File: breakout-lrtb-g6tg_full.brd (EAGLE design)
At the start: 27.9 x 14 mm, 11 parts

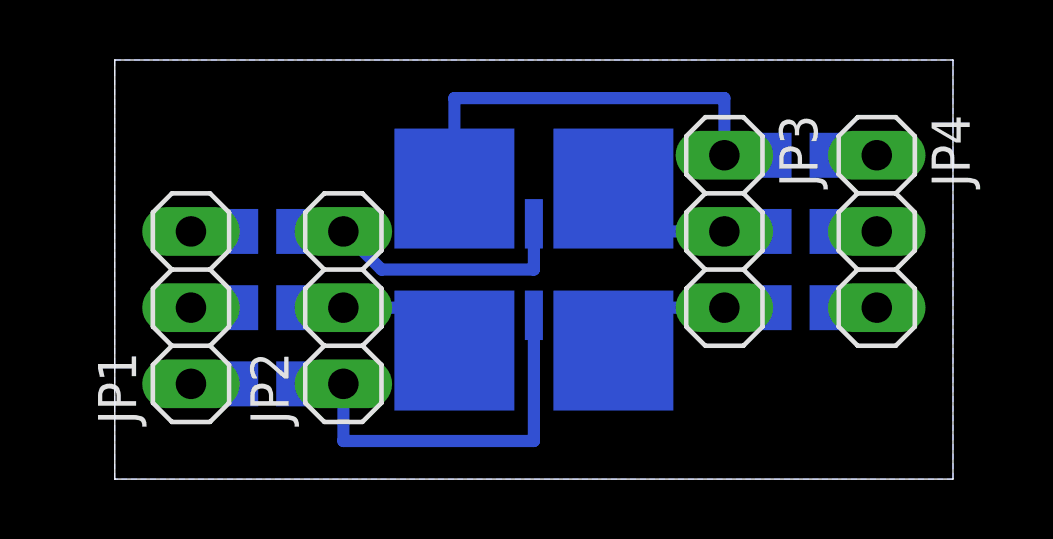
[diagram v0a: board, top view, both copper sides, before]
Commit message: another variant just with one pin for each pad
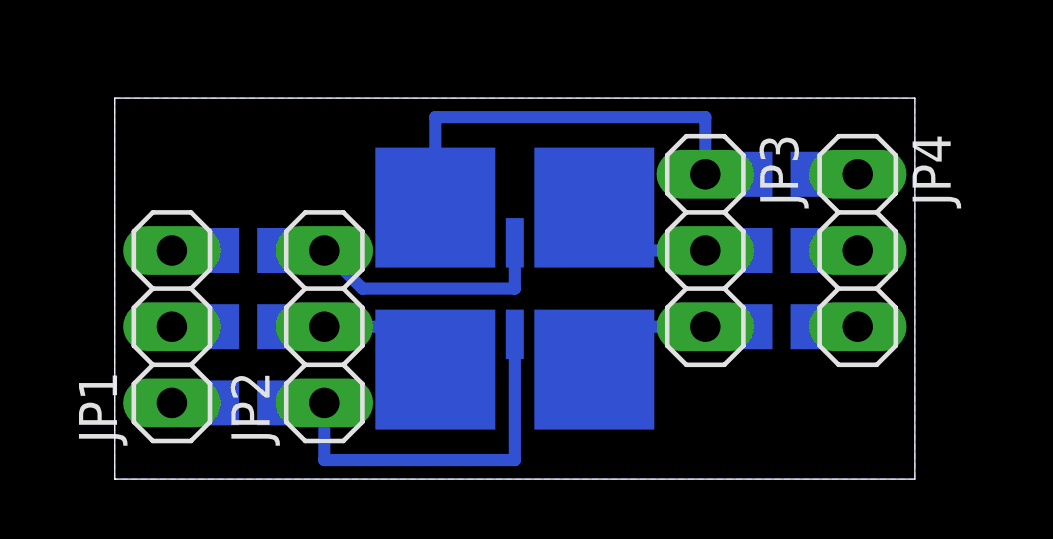
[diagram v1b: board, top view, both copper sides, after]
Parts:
- moved JP3 0.90 mm to (19.7, 7.62)
- moved LED1 0.90 mm to (13.3, 6.35)
- moved R1 0.90 mm to (4.45, 7.62)
- moved JP1 0.90 mm to (1.91, 5.08)
- moved JP2 0.90 mm to (6.99, 5.08)
- moved R2 0.90 mm to (4.45, 5.08)
- moved R3 0.90 mm to (4.45, 2.54)
- moved JP4 0.90 mm to (24.8, 7.62)
- moved R5 0.90 mm to (22.2, 7.62)
- moved R4 0.90 mm to (22.2, 5.08)
- moved R6 0.90 mm to (22.2, 10.2)
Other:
- board size 27.9 x 14 mm -> 26.7 x 12.7 mm
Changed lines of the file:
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@@
 <board>
 <plain>
-<wire x1="0" y1="0" x2="27.94" y2="0" width="0" layer="20"/>
-<wire x1="27.94" y1="0" x2="27.94" y2="13.97" width="0" layer="20"/>
-<wire x1="27.94" y1="13.97" x2="0" y2="13.97" width="0" layer="20"/>
-<wire x1="0" y1="13.97" x2="0" y2="0" width="0" layer="20"/>
-<rectangle x1="14.605" y1="6.35" x2="26.035" y2="7.62" layer="42"/>
-<rectangle x1="13.335" y1="9.525" x2="14.605" y2="12.065" layer="42"/>
-<rectangle x1="19.685" y1="8.89" x2="26.035" y2="10.16" layer="42"/>
-<rectangle x1="1.905" y1="6.35" x2="8.255" y2="7.62" layer="42"/>
-<rectangle x1="1.905" y1="3.81" x2="8.255" y2="5.08" layer="42"/>
+<wire x1="0" y1="0" x2="26.67" y2="0" width="0" layer="20"/>
+<wire x1="26.67" y1="0" x2="26.67" y2="12.7" width="0" layer="20"/>
+<wire x1="26.67" y1="12.7" x2="0" y2="12.7" width="0" layer="20"/>
+<wire x1="0" y1="12.7" x2="0" y2="0" width="0" layer="20"/>
+<rectangle x1="13.97" y1="5.715" x2="25.4" y2="6.985" layer="42"/>
+<rectangle x1="12.7" y1="8.89" x2="13.97" y2="11.43" layer="42"/>
+<rectangle x1="19.05" y1="8.255" x2="25.4" y2="9.525" layer="42"/>
+<rectangle x1="1.27" y1="5.715" x2="7.62" y2="6.985" layer="42"/>
+<rectangle x1="1.27" y1="3.175" x2="7.62" y2="4.445" layer="42"/>
+<rectangle x1="0.635" y1="1.27" x2="6.35" y2="1.905" layer="42"/>
+<rectangle x1="20.32" y1="11.43" x2="26.035" y2="12.065" layer="42"/>
 </plain>
 <attributes>
@@
 </autorouter>
 <elements>
-<element name="LED1" library="led" package="LRTB_G6SG" value="LRTB_G6SG" x="13.97" y="6.985" rot="MR180"/>
-<element name="JP1" library="pinhead" package="1X03" value="" x="2.54" y="5.715" rot="R90"/>
-<element name="JP2" library="pinhead" package="1X03" value="" x="7.62" y="5.715" rot="R90"/>
-<element name="JP3" library="pinhead" package="1X03" value="" x="20.32" y="8.255" rot="R270"/>
-<element name="JP4" library="pinhead" package="1X03" value="" x="25.4" y="8.255" rot="R270"/>
-<element name="R1" library="rcl" package="R0805" value="" x="5.08" y="8.255" rot="MR180"/>
-<element name="R2" library="rcl" package="R0805" value="" x="5.08" y="5.715" rot="MR180"/>
-<element name="R3" library="rcl" package="R0805" value="" x="5.08" y="3.175" rot="MR180"/>
-<element name="R4" library="rcl" package="R0805" value="" x="22.86" y="5.715" rot="MR180"/>
-<element name="R5" library="rcl" package="R0805" value="" x="22.86" y="8.255" rot="MR180"/>
-<element name="R6" library="rcl" package="R0805" value="" x="22.86" y="10.795" rot="MR180"/>
+<element name="LED1" library="led" package="LRTB_G6SG" value="LRTB_G6SG" x="13.335" y="6.35" rot="MR180"/>
+<element name="JP1" library="pinhead" package="1X03" value="" x="1.905" y="5.08" rot="R90"/>
+<element name="JP2" library="pinhead" package="1X03" value="" x="6.985" y="5.08" rot="R90"/>
+<element name="JP3" library="pinhead" package="1X03" value="" x="19.685" y="7.62" rot="R270"/>
+<element name="JP4" library="pinhead" package="1X03" value="" x="24.765" y="7.62" rot="R270"/>
+<element name="R1" library="rcl" package="R0805" value="" x="4.445" y="7.62" rot="MR180"/>
+<element name="R2" library="rcl" package="R0805" value="" x="4.445" y="5.08" rot="MR180"/>
+<element name="R3" library="rcl" package="R0805" value="" x="4.445" y="2.54" rot="MR180"/>
+<element name="R4" library="rcl" package="R0805" value="" x="22.225" y="5.08" rot="MR180"/>
+<element name="R5" library="rcl" package="R0805" value="" x="22.225" y="7.62" rot="MR180"/>
+<element name="R6" library="rcl" package="R0805" value="" x="22.225" y="10.16" rot="MR180"/>
 </elements>
 <signals>
@@
 <contactref element="JP4" pad="3"/>
 <contactref element="R4" pad="2"/>
-<wire x1="23.81" y1="5.715" x2="25.4" y2="5.715" width="0.6096" layer="16"/>
+<wire x1="23.175" y1="5.08" x2="24.765" y2="5.08" width="0.6096" layer="16"/>
 </signal>
 <signal name="N$2">
 <contactref element="JP4" pad="2"/>
 <contactref element="R5" pad="2"/>
-<wire x1="23.81" y1="8.255" x2="25.4" y2="8.255" width="0.6096" layer="16"/>
+<wire x1="23.175" y1="7.62" x2="24.765" y2="7.62" width="0.6096" layer="16"/>
 </signal>
 <signal name="N$3">
 <contactref element="JP4" pad="1"/>
 <contactref element="R6" pad="2"/>
-<wire x1="23.81" y1="10.795" x2="25.4" y2="10.795" width="0.6096" layer="16"/>
+<wire x1="23.175" y1="10.16" x2="24.765" y2="10.16" width="0.6096" layer="16"/>
 </signal>
 <signal name="N$4">
@@
 <contactref element="R5" pad="1"/>
 <contactref element="LED1" pad="3"/>
-<wire x1="21.91" y1="8.255" x2="20.32" y2="8.255" width="0.6096" layer="16"/>
-<wire x1="16.62" y1="9.685" x2="16.62" y2="8.255" width="0.4064" layer="16"/>
-<wire x1="16.62" y1="8.255" x2="20.32" y2="8.255" width="0.4064" layer="16"/>
+<wire x1="21.275" y1="7.62" x2="19.685" y2="7.62" width="0.6096" layer="16"/>
+<wire x1="15.985" y1="9.05" x2="15.985" y2="7.62" width="0.4064" layer="16"/>
+<wire x1="15.985" y1="7.62" x2="19.685" y2="7.62" width="0.4064" layer="16"/>
 </signal>
 <signal name="N$5">
@@
 <contactref element="R4" pad="1"/>
 <contactref element="LED1" pad="4"/>
-<wire x1="21.91" y1="5.715" x2="20.32" y2="5.715" width="0.6096" layer="16"/>
-<wire x1="16.62" y1="4.285" x2="16.62" y2="5.715" width="0.4064" layer="16"/>
-<wire x1="16.62" y1="5.715" x2="20.32" y2="5.715" width="0.4064" layer="16"/>
+<wire x1="21.275" y1="5.08" x2="19.685" y2="5.08" width="0.6096" layer="16"/>
+<wire x1="15.985" y1="3.65" x2="15.985" y2="5.08" width="0.4064" layer="16"/>
+<wire x1="15.985" y1="5.08" x2="19.685" y2="5.08" width="0.4064" layer="16"/>
 </signal>
 <signal name="N$6">
@@
 <contactref element="R6" pad="1"/>
 <contactref element="LED1" pad="1"/>
-<wire x1="21.91" y1="10.795" x2="20.32" y2="10.795" width="0.6096" layer="16"/>
-<wire x1="20.32" y1="10.795" x2="20.32" y2="12.7" width="0.4064" layer="16"/>
-<wire x1="20.32" y1="12.7" x2="11.32" y2="12.7" width="0.4064" layer="16"/>
-<wire x1="11.32" y1="12.7" x2="11.32" y2="9.685" width="0.4064" layer="16"/>
+<wire x1="21.275" y1="10.16" x2="19.685" y2="10.16" width="0.6096" layer="16"/>
+<wire x1="19.685" y1="10.16" x2="19.685" y2="12.065" width="0.4064" layer="16"/>
+<wire x1="19.685" y1="12.065" x2="10.685" y2="12.065" width="0.4064" layer="16"/>
+<wire x1="10.685" y1="12.065" x2="10.685" y2="9.05" width="0.4064" layer="16"/>
 </signal>
 <signal name="N$7">
 <contactref element="JP2" pad="2"/>
 <contactref element="R2" pad="2"/>
-<wire x1="6.03" y1="5.715" x2="7.62" y2="5.715" width="0.6096" layer="16"/>
+<wire x1="5.395" y1="5.08" x2="6.985" y2="5.08" width="0.6096" layer="16"/>
 <contactref element="LED1" pad="6"/>
-<wire x1="7.62" y1="5.715" x2="11.32" y2="5.715" width="0.4064" layer="16"/>
-<wire x1="11.32" y1="5.715" x2="11.32" y2="4.285" width="0.4064" layer="16"/>
+<wire x1="6.985" y1="5.08" x2="10.685" y2="5.08" width="0.4064" layer="16"/>
+<wire x1="10.685" y1="5.08" x2="10.685" y2="3.65" width="0.4064" layer="16"/>
 </signal>
 <signal name="N$8">
@@
 <contactref element="LED1" pad="5"/>
 <contactref element="R3" pad="2"/>
-<wire x1="6.03" y1="3.175" x2="7.62" y2="3.175" width="0.6096" layer="16"/>
-<wire x1="13.97" y1="5.46" x2="13.97" y2="1.27" width="0.4064" layer="16"/>
-<wire x1="13.97" y1="1.27" x2="7.62" y2="1.27" width="0.4064" layer="16"/>
-<wire x1="7.62" y1="1.27" x2="7.62" y2="3.175" width="0.4064" layer="16"/>
+<wire x1="5.395" y1="2.54" x2="6.985" y2="2.54" width="0.6096" layer="16"/>
+<wire x1="13.335" y1="4.825" x2="13.335" y2="0.635" width="0.4064" layer="16"/>
+<wire x1="13.335" y1="0.635" x2="6.985" y2="0.635" width="0.4064" layer="16"/>
+<wire x1="6.985" y1="0.635" x2="6.985" y2="2.54" width="0.4064" layer="16"/>
 </signal>
 <signal name="N$10">
 <contactref element="JP1" pad="2"/>
 <contactref element="R2" pad="1"/>
-<wire x1="4.13" y1="5.715" x2="2.54" y2="5.715" width="0.6096" layer="16"/>
+<wire x1="3.495" y1="5.08" x2="1.905" y2="5.08" width="0.6096" layer="16"/>
 </signal>
 <signal name="N$11">
 <contactref element="JP1" pad="1"/>
 <contactref element="R3" pad="1"/>
-<wire x1="4.13" y1="3.175" x2="2.54" y2="3.175" width="0.6096" layer="16"/>
+<wire x1="3.495" y1="2.54" x2="1.905" y2="2.54" width="0.6096" layer="16"/>
 </signal>
 <signal name="N$12">
 <contactref element="JP1" pad="3"/>
 <contactref element="R1" pad="1"/>
-<wire x1="4.13" y1="8.255" x2="2.54" y2="8.255" width="0.6096" layer="16"/>
+<wire x1="3.495" y1="7.62" x2="1.905" y2="7.62" width="0.6096" layer="16"/>
 </signal>
 <signal name="N$9">
@@
 <contactref element="R1" pad="2"/>
 <contactref element="LED1" pad="2"/>
-<wire x1="6.03" y1="8.255" x2="7.62" y2="8.255" width="0.6096" layer="16"/>
-<wire x1="13.97" y1="8.51" x2="13.97" y2="6.985" width="0.4064" layer="16"/>
-<wire x1="13.97" y1="6.985" x2="8.89" y2="6.985" width="0.4064" layer="16"/>
-<wire x1="8.89" y1="6.985" x2="7.62" y2="8.255" width="0.4064" layer="16"/>
+<wire x1="5.395" y1="7.62" x2="6.985" y2="7.62" width="0.6096" layer="16"/>
+<wire x1="13.335" y1="7.875" x2="13.335" y2="6.35" width="0.4064" layer="16"/>
+<wire x1="13.335" y1="6.35" x2="8.255" y2="6.35" width="0.4064" layer="16"/>
+<wire x1="8.255" y1="6.35" x2="6.985" y2="7.62" width="0.4064" layer="16"/>
 </signal>
 <signal name="N$13">
 <polygon width="0.4064" layer="16">
-<vertex x="27.94" y="13.97"/>
-<vertex x="27.94" y="0"/>
+<vertex x="26.67" y="12.7"/>
+<vertex x="26.67" y="0"/>
 <vertex x="0" y="0"/>
-<vertex x="0" y="13.97"/>
+<vertex x="0" y="12.7"/>
 </polygon>
 </signal>
